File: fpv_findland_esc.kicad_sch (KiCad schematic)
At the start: 45 parts, among them J13 Conn_01x06, U9 ST732M50R

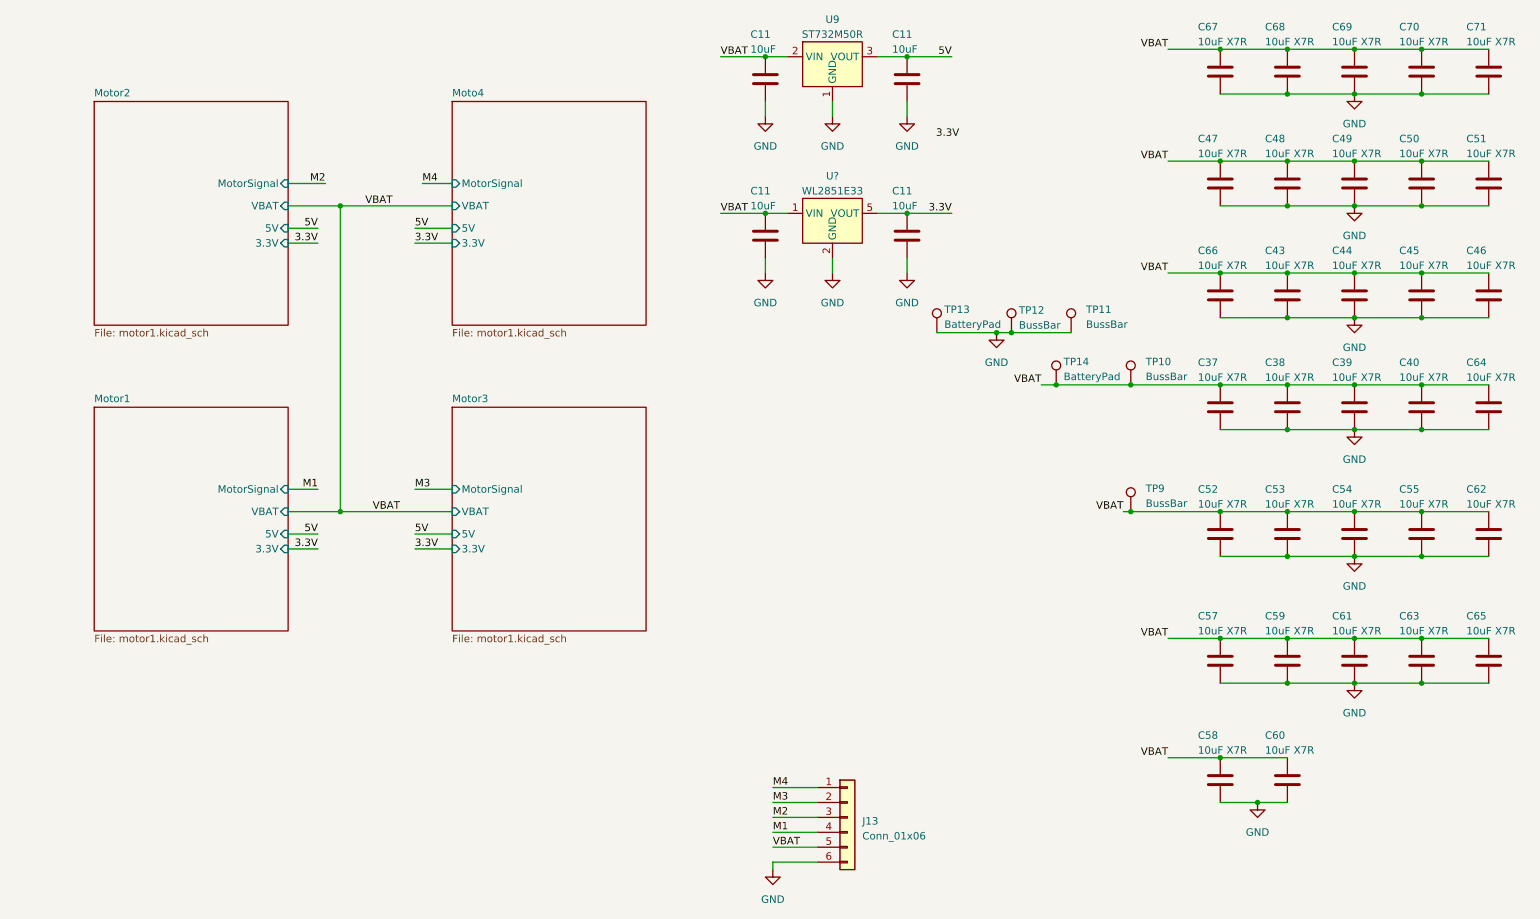
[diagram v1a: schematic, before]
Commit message: Moved top layer fets to allow more current. Other small improvements.
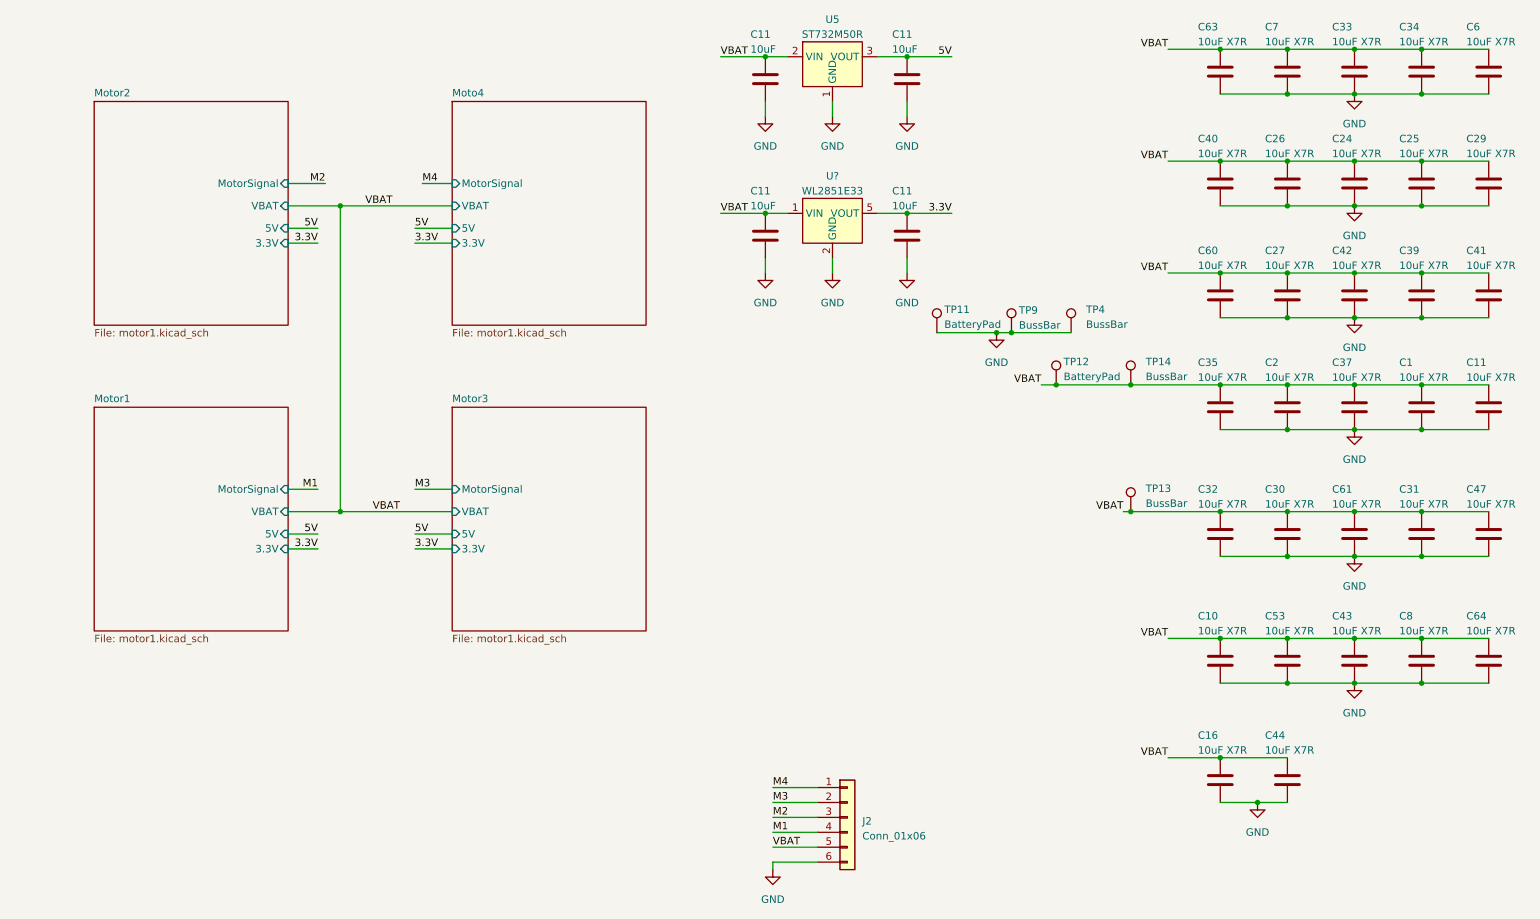
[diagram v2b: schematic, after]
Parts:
- J2: renamed from J13; now left out of the parts list
- TP11: renamed from TP13; now left out of the parts list
- TP12: renamed from TP14; now left out of the parts list
- TP13: renamed from TP9; now left out of the parts list
- TP14: renamed from TP10; now left out of the parts list
- TP4: renamed from TP11; now left out of the parts list
- TP9: renamed from TP12; now left out of the parts list
- U5: renamed from U9; LCSC (none) -> https://www.lcsc.com/product-detail/Linear-Voltage-Regulato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; LSCS https://www.lcsc.com/product-detail/Linear-Voltage-Regulato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 -> (none)
- U?: LCSC (none) -> https://www.lcsc.com/product-detail/Linear-Voltage-Regulato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; LSCS https://www.lcsc.com/product-detail/Linear-Voltage-Regulato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 -> (none)
- renumbered C40 to C1, C57 to C10, C64 to C11, C58 to C16, C38 to C2, C49 to C24, C50 to C25, C48 to C26, C43 to C27, C51 to C29, C53 to C30, C55 to C31, C52 to C32, C69 to C33, C70 to C34, C37 to C35, C39 to C37, C45 to C39, C47 to C40, C46 to C41, C44 to C42, C61 to C43, C60 to C44, C62 to C47, C59 to C53, C71 to C6, C66 to C60, C54 to C61, C67 to C63, C65 to C64, C68 to C7, C63 to C8

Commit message: Updated power supply scheme. 10V step down to a 3.3V LDO.
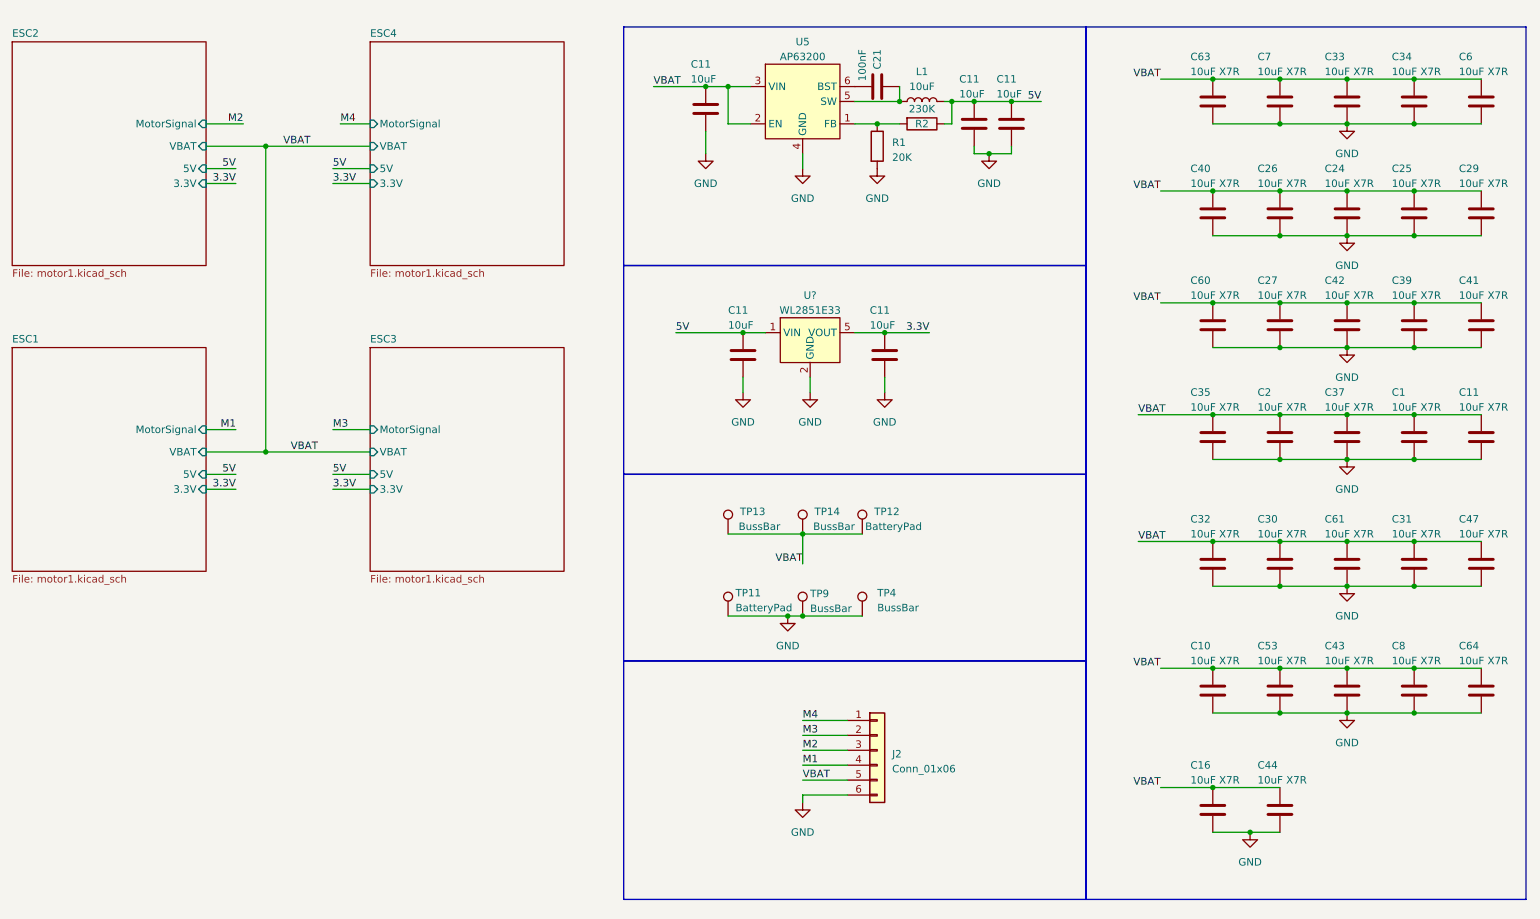
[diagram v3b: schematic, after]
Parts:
- removed C11 (x2): 10uF, Capacitor_SMD:C_0603_1608Metric, symbol Device:C
- removed U5: ST732M50R, OpenHW:SOT-23-5, symbol OpenHW:ST732M50R
- added C11 (x3): 10uF, Capacitor_SMD:C_0603_1608Metric, symbol Device:C
- added C21: 100nF, Capacitor_SMD:C_0402_1005Metric, symbol Device:C
- added L1: 10uF, Capacitor_SMD:C_0805_2012Metric, symbol Device:L
- added R1: 20K, Resistor_SMD:R_0402_1005Metric, symbol Device:R
- added R2: 230K, Resistor_SMD:R_0402_1005Metric, symbol Device:R
- added U5: AP63200, OpenHW:SOT-23-6, symbol OpenHW:AP63200
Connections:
- net 5V: now also C11.1, U?.1 (VIN), C11.1, C11.1, L1.2, R2.1
- net GND: now also C11.2, C11.2, C11.2, R1.2, U5.4 (GND)
- net VBAT: now also C11.1, U5.2 (EN), U5.3 (VIN); no longer C11.1, U?.1 (VIN)
- new net: C21.1, L1.1, U5.5 (SW)
- new net: C21.2, U5.6 (BST)
- new net: R1.1, R2.2, U5.1 (FB)
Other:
- sheet Moto4 renamed ESC4
- sheet Motor1 renamed ESC1
- sheet Motor2 renamed ESC2
- sheet Motor3 renamed ESC3
- moved on the sheet: C1, C10, C11, C16, C2, C24, C25, C26, C27, C29, C30, C31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

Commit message: Removed unneccessary islands etc.
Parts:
- TP13, TP14: footprint OpenHW:2mmBussBar -> OpenHW:2mmBussBar33MM
- TP4, TP9: footprint OpenHW:2mmBussBar -> OpenHW:2mmBussBar36MM
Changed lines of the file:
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@@
       (effects (font (size 1.27 1.27)) (justify left))
     )
-    (property "Footprint" "OpenHW:2mmBussBar" (at 157.48 116.84 0)
+    (property "Footprint" "OpenHW:2mmBussBar36MM" (at 157.48 116.84 0)
       (effects (font (size 1.27 1.27)) hide)
     )
@@
       (effects (font (size 1.27 1.27)) (justify left))
     )
-    (property "Footprint" "OpenHW:2mmBussBar" (at 134.62 102.87 0)
+    (property "Footprint" "OpenHW:2mmBussBar33MM" (at 134.62 102.87 0)
       (effects (font (size 1.27 1.27)) hide)
     )
@@
       (effects (font (size 1.27 1.27)) (justify left))
     )
-    (property "Footprint" "OpenHW:2mmBussBar" (at 167.64 116.84 0)
+    (property "Footprint" "OpenHW:2mmBussBar36MM" (at 167.64 116.84 0)
       (effects (font (size 1.27 1.27)) hide)
     )
@@
       (effects (font (size 1.27 1.27)) (justify left))
     )
-    (property "Footprint" "OpenHW:2mmBussBar" (at 147.32 102.87 0)
-      (effects (font (size 1.27 1.27)) hide)
-    )
+    (property "Footprint" "OpenHW:2mmBussBar33MM" (at 147.32 102.87 0)
+      (effects (font (size 1.27 1.27)) hide)
+    )
